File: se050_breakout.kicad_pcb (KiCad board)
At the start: 2 copper layers, 16.3 x 12.7 mm, 10 parts, among them J1 Conn_01x05_Pin

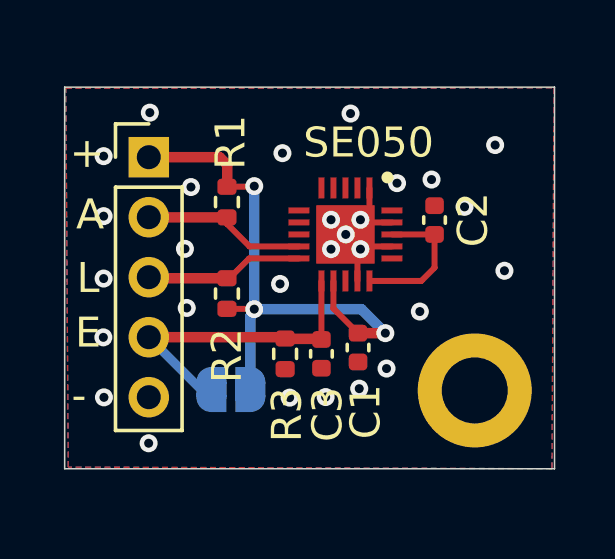
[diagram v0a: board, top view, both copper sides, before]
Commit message: Add assembly fiducials and refresh the fabrication output
The board grows to 16.42 x 14.56 mm to make room for two 1 mm fiducials placed
diagonally, each with a 3 mm keepout drawn as a rule area on the top copper so
the ground pour backs away and leaves an assembly camera a clean target. The
circuit is unchanged; this only makes the board usable for machine assembly.

Correct the LCSC part number on R1 and R2. Both carried C60491, which is a
100k resistor, so a machine-assembled board would have shipped with 100k
pull-ups on the I2C bus instead of 4k7 and the SE050 would not have answered.

Regenerate gerber/. It still held the August layout and no longer matched the
board, so anyone ordering from it would have received the wrong outline.

Bring the README in line with the board: the bill of materials had a stale C2
and C3 from before the VOUT/VCC capacitor was removed, and it now carries the
LCSC numbers, the fiducial notes, and an accurate account of what has and has
not been fabricated.
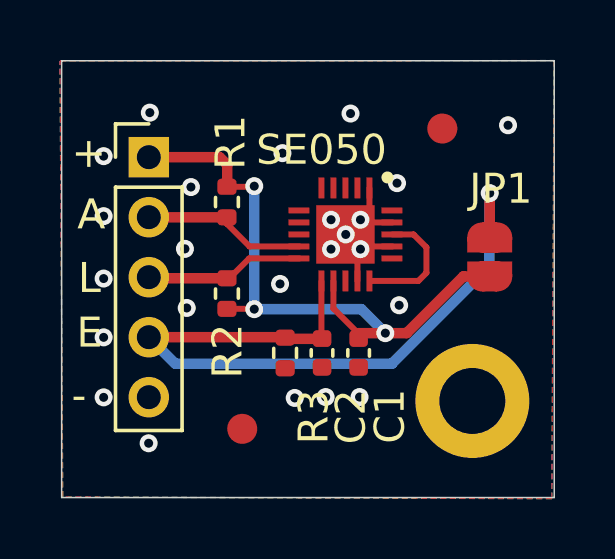
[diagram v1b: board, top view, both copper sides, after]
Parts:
- removed C3: 33nF, Capacitor_SMD:C_0402_1005Metric
- added FID1: Fiducial, Fiducial:Fiducial_1mm_Mask2mm, F.Cu at (124.2, 72.9)
- added FID2: Fiducial, Fiducial:Fiducial_1mm_Mask2mm, F.Cu at (117.5, 82.9)
- JP1: moved to F.Cu
- moved JP1 9.70 mm to (125.8, 77.2), turned to -90 degrees
- moved C2 5.80 mm to (120.2, 80.4), turned to -90 degrees
- moved H1 0.36 mm to (125.2, 82.0)
- moved C1 0.18 mm to (121.4, 80.4)
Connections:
- C2 pad 1: Net-(SE050-VCC) -> SE050_ENA
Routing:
- net SE050_ENA: track 10.5 -> 24.7 mm, vias 0 -> 1
- net +3.3V: track 19.8 -> 21.4 mm
- net Net-(SE050-VCC): track 4.86 -> 4.17 mm
- net GND: vias 28 -> 24
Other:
- board size 16.3 x 12.7 mm -> 16.4 x 14.6 mm
